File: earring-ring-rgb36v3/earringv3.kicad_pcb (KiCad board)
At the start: 2 copper layers, 108 x 123.5 mm, 70 parts, among them J1 Conn_01x05, Q1 AO3401A, SW1 SW_Push, SW2 SW_Push, U1 GMA2718H09-F42-4P, U2 STM32L031G6Ux

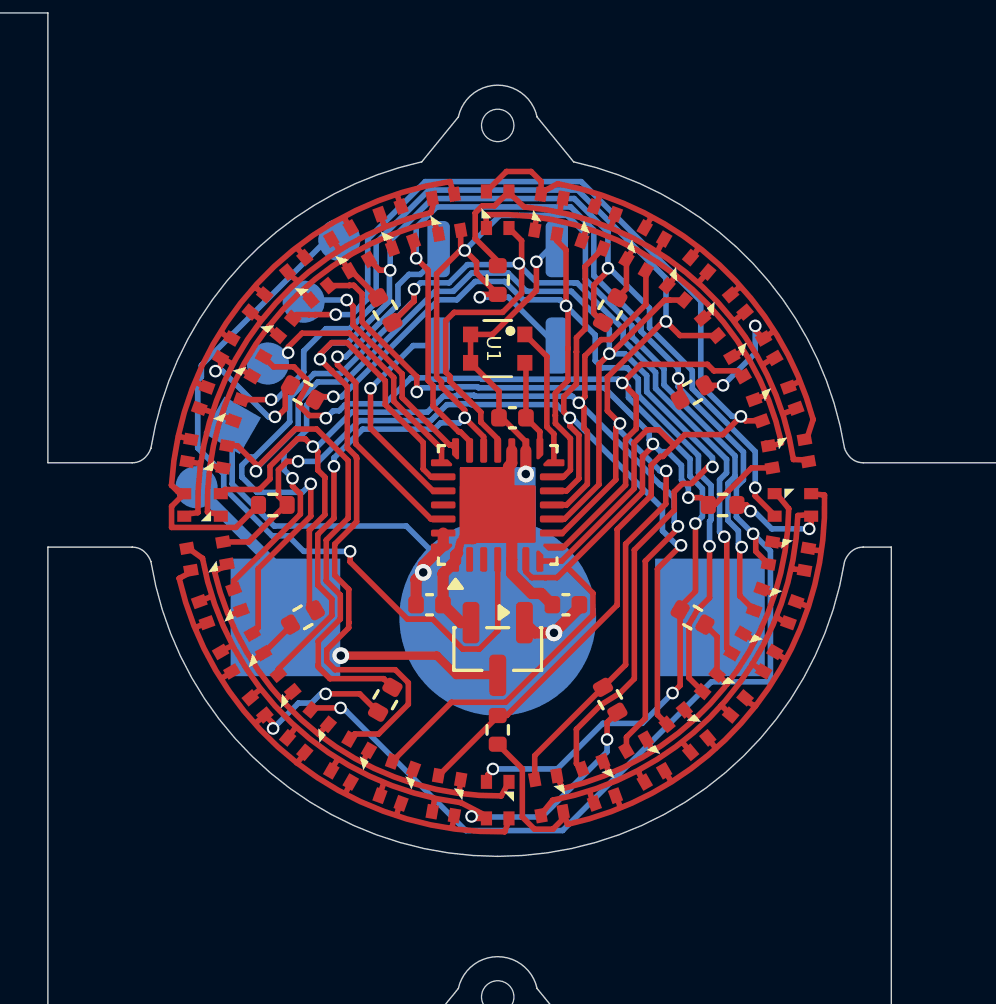
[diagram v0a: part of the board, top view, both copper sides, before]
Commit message: earring-ring-rgb36v3: schematic design for charlieplexing
This is the 3rd or 4th attempt, but the current schematic finally looks
usable.
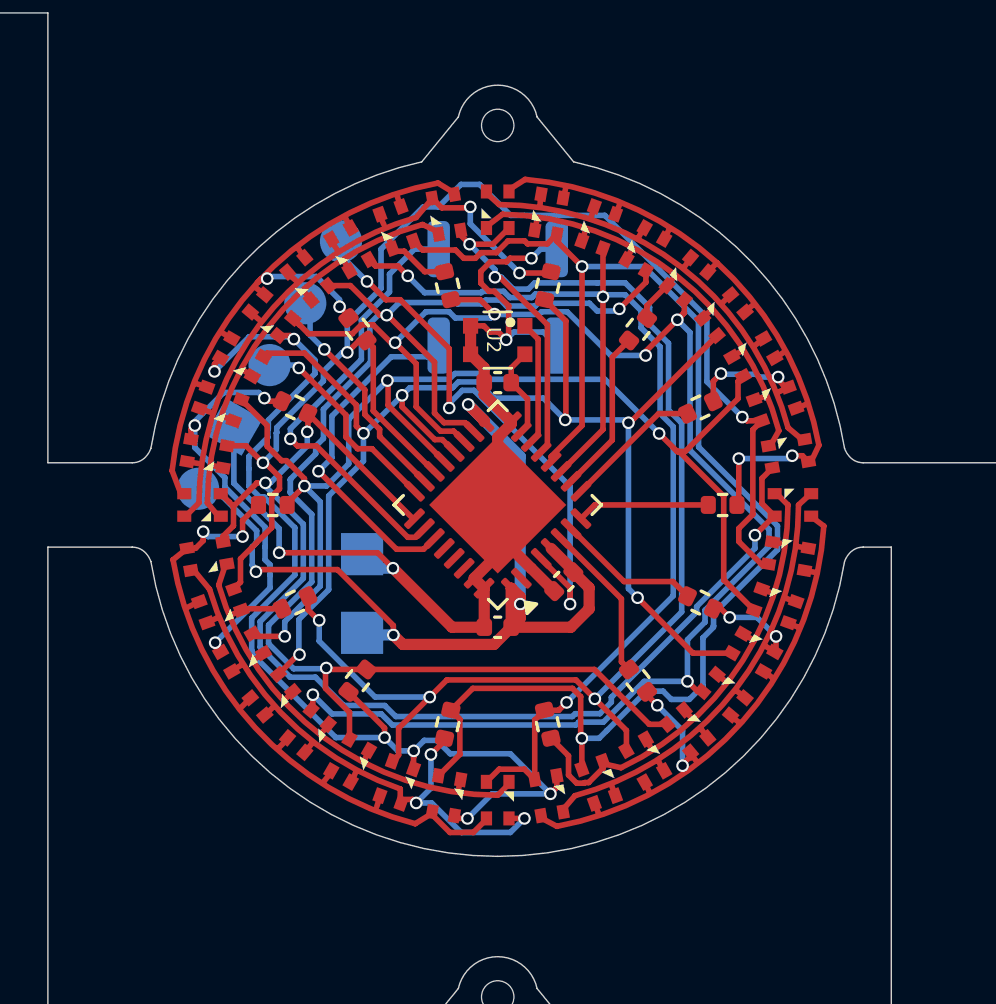
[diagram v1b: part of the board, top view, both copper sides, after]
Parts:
- removed BT1: Battery_Cell, Custom:MY-1220-03
- removed Q1: AO3401A, Package_TO_SOT_SMD:SOT-23
- removed the U2 at (0.00, 0.00)
- added R13: 1.5k, Resistor_SMD:R_0402_1005Metric, F.Cu at (7.21, 3.47)
- added R14: 330, Resistor_SMD:R_0402_1005Metric, F.Cu at (4.99, 6.25)
- added TP1: 3.0V, TestPoint:TestPoint_Pad_1.5x1.5mm, B.Cu at (-4.83, 4.55)
- added TP2: GND, TestPoint:TestPoint_Pad_1.5x1.5mm, B.Cu at (-4.83, 1.75)
- added U1: STM32U073KCUx, Package_DFN_QFN:QFN-32-1EP_5x5mm_P0.5mm_EP3.45x3.45mm, F.Cu at (0.00, 0.00)
- R1, R2: value 1k -> 330
- R10, R11, R4, R5, R7, R8: value 1k -> 1.5k
- R12, R3: value 220 -> 330
- R6, R9: value 220 -> 1.5k
- moved R11 13.5 mm to (7.21, -3.47), turned to 25.71 degrees
- moved R2 12.1 mm to (-4.99, -6.25), turned to 128.57 degrees
- moved R1 11.7 mm to (-7.21, -3.47), turned to 154.29 degrees
- moved R3 11.3 mm to (-8.00, 0.00), turned to 180 degrees
- moved R10 10.4 mm to (4.99, -6.25), turned to 51.43 degrees
- moved R6 6.94 mm to (-4.99, 6.25), turned to -128.57 degrees
- moved R5 6.40 mm to (-1.78, -7.80), turned to 102.86 degrees
- moved R4 5.85 mm to (1.78, -7.80), turned to 77.14 degrees
- moved C1 2.55 mm to (0.00, 4.35)
- moved R8 2.38 mm to (-1.78, 7.80), turned to -102.86 degrees
- moved R9 2.38 mm to (1.78, 7.80), turned to -77.14 degrees
- moved C2 1.36 mm to (0.00, -4.35)
- moved C3 0.83 mm to (2.35, 2.73), turned to -135 degrees
- moved R7 0.60 mm to (-7.21, 3.47), turned to -154.29 degrees
- moved U2 0.31 mm to (0.00, -5.87)
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- renumbered U1 to U2
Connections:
- D1 pad 1: A4 -> A7
- D1 pad 2: A1R -> A10R
- D1 pad 3: A2R -> A11G
- D1 pad 4: A3R -> A12B
- D10 pad 2: A10R -> A9R
- D10 pad 3: A11R -> A13G
- D10 pad 4: A12R -> A14B
- D11 pad 2: A10R -> A9R
- D11 pad 3: A11R -> A13G
- D11 pad 4: A12R -> A14B
- D12 pad 2: A10R -> A9R
- D12 pad 3: A11R -> A13G
- D12 pad 4: A12R -> A14B
- D13 pad 2: A10R -> A9R
- D13 pad 3: A11R -> A13G
- D13 pad 4: A12R -> A14B
- D14 pad 2: A10R -> A9R
- D14 pad 3: A11R -> A13G
- D14 pad 4: A12R -> A14B
- D15 pad 2: A10R -> A9R
- D15 pad 3: A11R -> A13G
- D15 pad 4: A12R -> A14B
- D16 pad 2: A10R -> A9R
- D16 pad 3: A11R -> A13G
- D16 pad 4: A12R -> A14B
- D17 pad 2: A10R -> A9R
- D17 pad 3: A11R -> A13G
- D17 pad 4: A12R -> A14B
- D18 pad 2: A10R -> A6RG
- D18 pad 3: A11R -> A13G
- D18 pad 4: A12R -> A14B
- D19 pad 1: A10 -> A9
- D19 pad 3: A8R -> A8G
- D19 pad 4: A9R -> A3B
- D2 pad 1: A5 -> A8
- D2 pad 2: A1R -> A10R
- D2 pad 3: A2R -> A11G
- D2 pad 4: A3R -> A12B
- D20 pad 1: A11 -> A8
- D20 pad 3: A8R -> A6RG
- D20 pad 4: A9R -> A3B
- D21 pad 1: A12 -> A7
- D21 pad 2: A7R -> A6RG
- D21 pad 3: A8R -> A8G
- D21 pad 4: A9R -> A3B
- D22 pad 1: A1 -> A6
- D22 pad 3: A8R -> A8G
- D22 pad 4: A9R -> A3B
- D23 pad 1: A2 -> A5
- D23 pad 3: A8R -> A8G
- D23 pad 4: A9R -> A3B
- D24 pad 1: A3 -> A4
- D24 pad 3: A8R -> A8G
- D24 pad 4: A9R -> A3B
- D25 pad 1: A4 -> A3
- D25 pad 3: A8R -> A8G
- D25 pad 4: A9R -> A1B
- D26 pad 1: A5 -> A2
- D26 pad 3: A8R -> A8G
- D26 pad 4: A9R -> A3B
- D27 pad 1: A6 -> A1
- D27 pad 3: A8R -> A8G
- D27 pad 4: A9R -> A3B
- D28 pad 1: A7 -> A1
- D28 pad 2: A4R -> A5R
- D28 pad 3: A5R -> A4G
- D28 pad 4: A6R -> A2B
- D29 pad 1: A8 -> A2
- D29 pad 2: A4R -> A5R
- D29 pad 3: A5R -> A4G
- D29 pad 4: A6R -> A1B
- D3 pad 1: A6 -> A9
- D3 pad 2: A1R -> A10R
- D3 pad 3: A2R -> A11G
- D3 pad 4: A3R -> A12B
- D30 pad 1: A9 -> A3
- D30 pad 2: A4R -> A5R
- D30 pad 3: A5R -> A4G
- D30 pad 4: A6R -> A2B
- D31 pad 1: A10 -> A4
- D31 pad 2: A4R -> A5R
- D31 pad 3: A5R -> A6RG
- D31 pad 4: A6R -> A2B
- D32 pad 1: A11 -> A5
- D32 pad 2: A4R -> A6RG
- D32 pad 3: A5R -> A4G
- D32 pad 4: A6R -> A2B
- D33 pad 1: A12 -> A6
- D33 pad 2: A4R -> A5R
- D33 pad 3: A5R -> A4G
- D33 pad 4: A6R -> A2B
- D34 pad 1: A1 -> A9
- D34 pad 2: A4R -> A5R
- D34 pad 3: A5R -> A4G
- D34 pad 4: A6R -> A2B
- D35 pad 1: A2 -> A8
- D35 pad 2: A4R -> A5R
- D35 pad 3: A5R -> A4G
- D35 pad 4: A6R -> A2B
- D36 pad 1: A3 -> A7
- D36 pad 2: A4R -> A5R
- D36 pad 3: A5R -> A4G
- D36 pad 4: A6R -> A2B
- D4 pad 1: A7 -> A6
- D4 pad 2: A1R -> A10R
- D4 pad 3: A2R -> A11G
- D4 pad 4: A3R -> A12B
- D5 pad 1: A8 -> A5
- D5 pad 2: A1R -> A10R
- D5 pad 3: A2R -> A11G
- D5 pad 4: A3R -> A12B
- D6 pad 1: A9 -> A4
- D6 pad 2: A1R -> A10R
- D6 pad 3: A2R -> A11G
- D6 pad 4: A3R -> A12B
- D7 pad 1: A10 -> A3
- D7 pad 2: A1R -> A10R
- D7 pad 3: A2R -> A11G
- D7 pad 4: A3R -> A12B
- D8 pad 1: A11 -> A2
- D8 pad 2: A1R -> A10R
- D8 pad 3: A2R -> A11G
- D8 pad 4: A3R -> A12B
- D9 pad 1: A12 -> A1
- D9 pad 2: A1R -> A10R
- D9 pad 3: A2R -> A11G
- D9 pad 4: A3R -> A12B
- J1 pad 1: VBAT -> VCC
- R1 pad 1: A1R -> A1
- R1 pad 2: A1 -> A1B
- R11 pad 2: A11R -> A11G
- R12 pad 2: A12R -> A12B
- R2 pad 2: A2R -> A2B
- R3 pad 2: A3R -> A3B
- R4 pad 2: A4R -> A4G
- R6 pad 2: A6R -> A6RG
- R8 pad 2: A8R -> A8G
- SW1 pad 2: Net-(U2-PB7) -> BTN_MODE
- SW2 pad 1: A3 -> GND
- SW2 pad 2: Net-(U2-PB3) -> BTN_COLOR
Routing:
- net A11: track 51.4 -> 4.93 mm, vias 2 -> 0
- net A10: track 47.6 -> 5.87 mm, vias 5 -> 0
- net A6RG: track 0.00 -> 38.8 mm, vias 0 -> 6
- net A12: track 40.5 -> 4.73 mm, vias 3 -> 0
- net VCC: track 10.2 -> 33.6 mm, vias 0 -> 4
- net BTN_MODE: track 0.00 -> 15.8 mm, vias 0 -> 1
- net A1B: track 0.00 -> 14.4 mm, vias 0 -> 3
- net VBAT: track 14.1 -> 0.00 mm, vias 1 -> 0
- net Net-(U2-PB7): track 13.9 -> 0.00 mm, vias 1 -> 0
- net A8: track 63.7 -> 50.6 mm, vias 3 -> 2
- net A1: track 56.7 -> 43.9 mm, vias 4 -> 3
- net A6: track 39.0 -> 51.5 mm
- net BTN_COLOR: track 0.00 -> 12.4 mm, vias 0 -> 1
- net A2: track 57.7 -> 48.3 mm, vias 4 -> 3
- net A9: track 50.0 -> 40.7 mm, vias 4 -> 3
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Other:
- board text added: "3V"
- board text added: "G"
- board text added: "TODO: reduce diameter from 25mm to 24.5mm"
- board text added: "v3.0a"
- board text removed: "CR1225"
- board text removed: "v1.2"

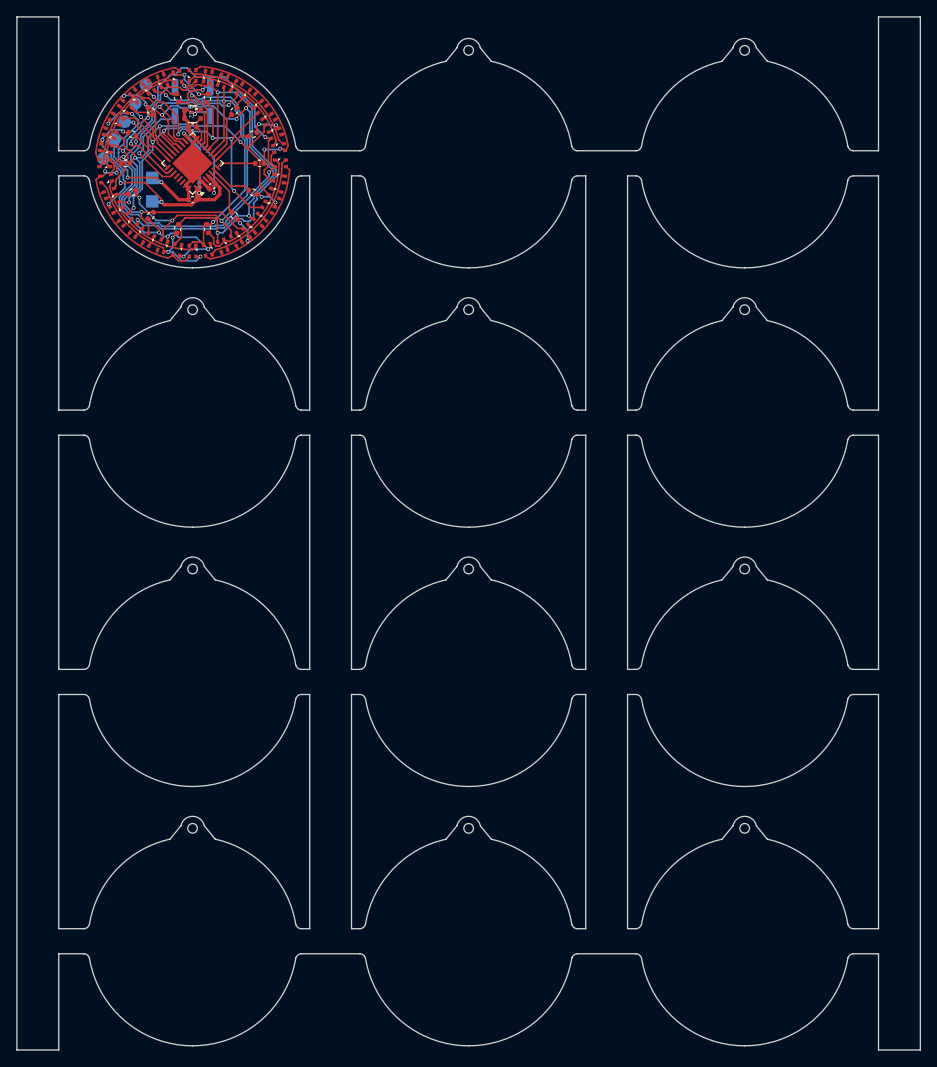
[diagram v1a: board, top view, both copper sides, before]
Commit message: earring-ring-rgb36v3: shrink from 25mm to 24mm
Also use bezier curve for the earring hook ring, this looks much nicer.
And remove the panel, we'll have to recreate it anyway with the smaller
PCB.
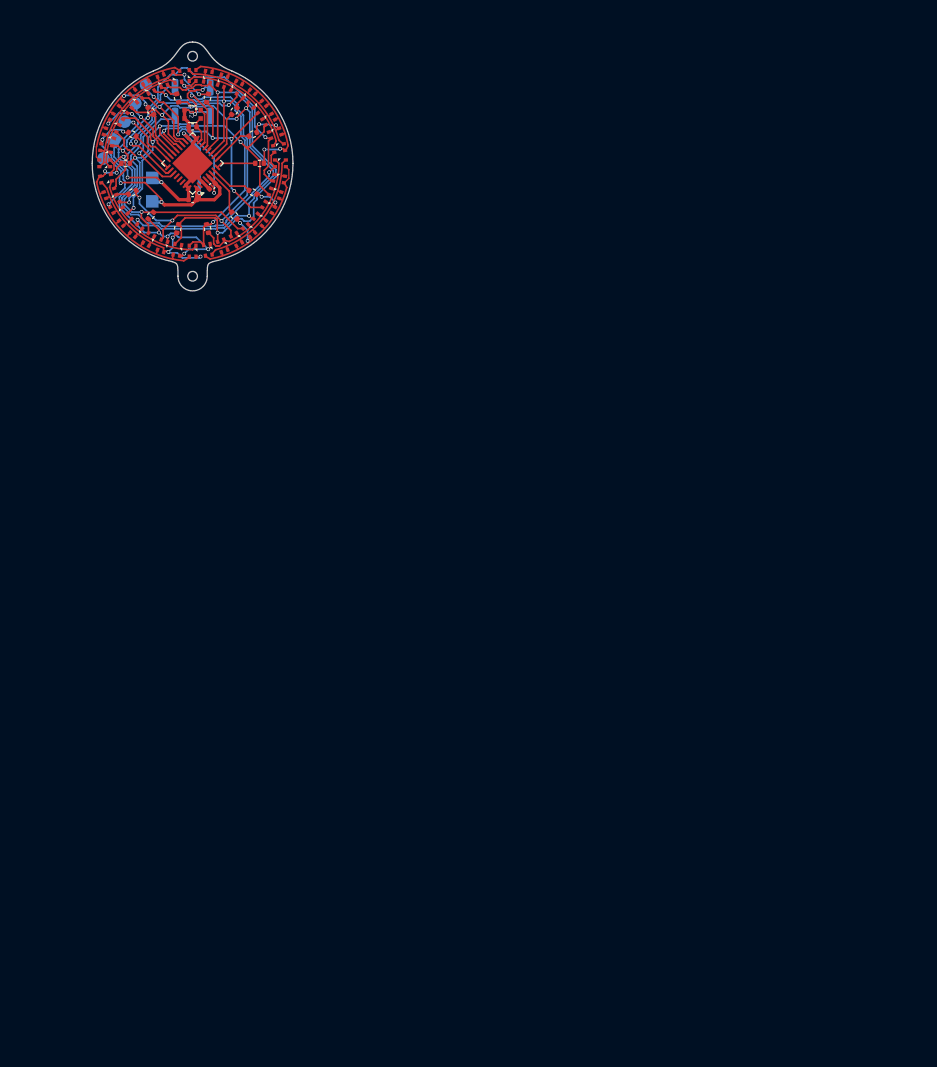
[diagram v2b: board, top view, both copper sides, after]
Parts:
- removed the H1 at (66.0, 17.5)
- removed the H1 at (33.0, 17.5)
- removed the H1 at (33.0, 79.5)
- removed the H1 at (0.00, 48.5)
- removed the H1 at (66.0, 79.5)
- removed the H1 at (33.0, -13.5)
- removed the H1 at (0.00, 79.5)
- removed the H1 at (0.00, 17.5)
- removed the H1 at (66.0, -13.5)
- removed the H1 at (33.0, 48.5)
- removed the H1 at (66.0, 48.5)
- added H1: ToolingHole, Custom:ToolingHole_JLCPCB, F.Cu at (0.00, 13.5)
- moved H1 0.70 mm to (0.00, -12.8)
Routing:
- net A3B: track 6.38 -> 3.85 mm
- net A14B: track 3.66 -> 6.02 mm
- net A2B: track 4.14 -> 5.90 mm
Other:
- board size 108 x 123.5 mm -> 24 x 29.8 mm
- board text added: "color/program"
- board text added: "power"
- board text removed: "TODO: reduce diameter from 25mm to 24.5mm"
- board text removed: "V-cut"
- board text removed: "color/ program"
- board text removed: "mode/power"

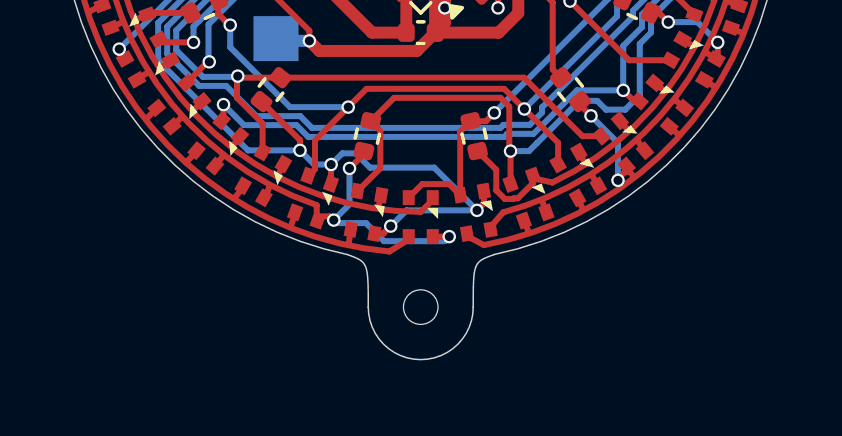
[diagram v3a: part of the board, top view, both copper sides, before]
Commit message: earring-ring-rgb36v3: mouse bytes at bottom tooling hole
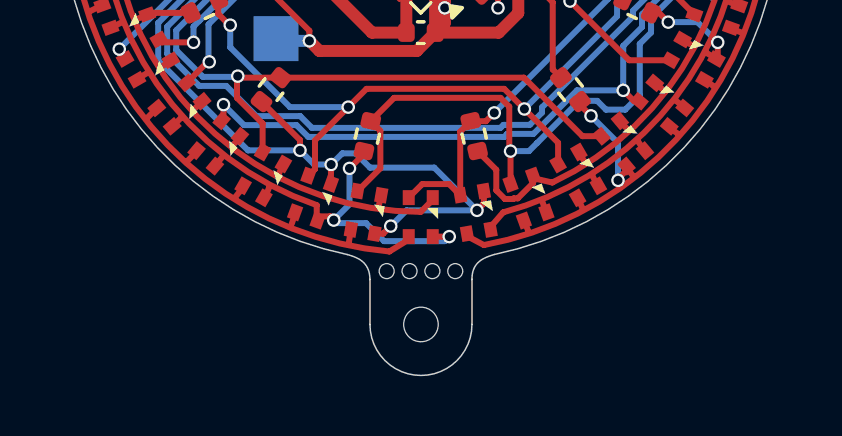
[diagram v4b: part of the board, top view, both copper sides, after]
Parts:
- removed the H1 at (0.00, 13.5)
- added REF**: ToolingHoleWithMouseBytes, Custom:ToolingHoleWithMouseBytes, F.Cu at (0.01, 14.1)
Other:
- board size 24 x 29.8 mm -> 24 x 27.1 mm
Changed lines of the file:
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@@
 		)
 	)
+	(footprint "Custom:ToolingHoleWithMouseBytes"
+		(layer "F.Cu")
+		(at 0.007 14.078)
+		(property "Reference" "REF**"
+			(at 0 -5.1 0)
+			(unlocked yes)
+			(layer "F.SilkS")
+			(hide yes)
+			(effects
+				(font
+					(size 1 1)
+					(thickness 0.1)
+				)
+			)
+		)
+		(property "Value" "ToolingHoleWithMouseBytes"
+			(at 0 -3.6 0)
+			(unlocked yes)
+			(layer "F.Fab")
+			(hide yes)
+			(effects
+				(font
+					(size 1 1)
+					(thickness 0.15)
+				)
+			)
+		)
+		(property "Datasheet" ""
+			(at 0 0 0)
+			(unlocked yes)
+			(layer "F.Fab")
+			(hide yes)
+			(effects
+				(font
+					(size 1 1)
+					(thickness 0.15)
+				)
+			)
+		)
+		(property "Description" ""
+			(at 0 0 0)
+			(unlocked yes)
+			(layer "F.Fab")
+			(hide yes)
+			(effects
+				(font
+					(size 1 1)
+					(thickness 0.15)
+				)
+			)
+		)
+		(attr through_hole board_only)
+		(fp_line
+			(start -1.7 0)
+			(end -1.7 -1.5)
+			(stroke
+				(width 0.05)
+				(type default)
+			)
+			(layer "Edge.Cuts")
+		)
+		(fp_line
+			(start 1.7 0)
+			(end 1.7 -1.5)
+			(stroke
+				(width 0.05)
+				(type default)
+			)
+			(layer "Edge.Cuts")
+		)
+		(fp_arc
+			(start 1.7 0)
+			(mid 0 1.7)
+			(end -1.7 0)
+			(stroke
+				(width 0.05)
+				(type default)
+			)
+			(layer "Edge.Cuts")
+		)
+		(pad "" np_thru_hole circle
+			(at -1.143 -1.778)
+			(size 0.5 0.5)
+			(drill 0.5)
+			(layers "*.Mask")
+		)
+		(pad "" np_thru_hole circle
+			(at -0.381 -1.778)
+			(size 0.5 0.5)
+			(drill 0.5)
+			(layers "*.Mask")
+		)
+		(pad "" np_thru_hole circle
+			(at 0 0)
+			(size 1.152 1.152)
+			(drill 1.152)
+			(layers "*.Mask")
+			(solder_mask_margin 0.148)
+			(clearance 0.248)
+		)
+		(pad "" np_thru_hole circle
+			(at 0.381 -1.778)
+			(size 0.5 0.5)
+			(drill 0.5)
+			(layers "*.Mask")
+		)
+		(pad "" np_thru_hole circle
+			(at 1.143 -1.778)
+			(size 0.5 0.5)
+			(drill 0.5)
+			(layers "*.Mask")
+		)
+		(embedded_fonts no)
+	)
 	(footprint "Custom:NH-Z1415RGBA-SG"
 		(layer "F.Cu")
@@
 		)
 	)
-	(footprint "Custom:ToolingHole_JLCPCB"
-		(layer "F.Cu")
-		(at 0 13.5)
-		(property "Reference" "H1"
-			(at 0 -0.5 0)
-			(unlocked yes)
-			(layer "F.SilkS")
-			(hide yes)
-			(effects
-				(font
-					(size 1 1)
-					(thickness 0.1)
-				)
-			)
-		)
-		(property "Value" "ToolingHole"
-			(at 0 1 0)
-			(unlocked yes)
-			(layer "F.Fab")
-			(hide yes)
-			(effects
-				(font
-					(size 1 1)
-					(thickness 0.15)
-				)
-			)
-		)
-		(property "Datasheet" ""
-			(at 0 0 0)
-			(unlocked yes)
-			(layer "F.Fab")
-			(hide yes)
-			(effects
-				(font
-					(size 1 1)
-					(thickness 0.15)
-				)
-			)
-		)
-		(property "Description" "Mounting Hole without connection"
-			(at 0 0 0)
-			(unlocked yes)
-			(layer "F.Fab")
-			(hide yes)
-			(effects
-				(font
-					(size 1 1)
-					(thickness 0.15)
-				)
-			)
-		)
-		(attr through_hole board_only exclude_from_pos_files exclude_from_bom)
-		(pad "" np_thru_hole circle
-			(at 0 0)
-			(size 1.152 1.152)
-			(drill 1.152)
-			(layers "*.Mask")
-			(solder_mask_margin 0.148)
-			(clearance 0.248)
-		)
-		(embedded_fonts no)
-	)
 	(footprint "Custom:NH-Z1415RGBA-SG"
 		(layer "F.Cu")
@@
 		(end -11.6 3.9)
 		(stroke
-			(width 0.1)
+			(width 0.001)
 			(type default)
 		)
@@
 		(end 11.6 2.7)
 		(stroke
-			(width 0.1)
+			(width 0.001)
 			(type default)
 		)
@@
 	(gr_curve
 		(pts
-			(xy -1.75 13.5) (xy -1.75 12) (xy -1.75 12) (xy -2.447451 11.747764)
+			(xy -1.693 12.578) (xy -1.7 12) (xy -2.086 11.85) (xy -2.447446 11.747765)
 		)
 		(stroke
@@
 		(layer "Edge.Cuts")
 	)
-	(gr_arc
-		(start 1.75 13.5)
-		(mid 0 15.25)
-		(end -1.75 13.5)
-		(stroke
-			(width 0.05)
-			(type default)
-		)
-		(layer "Edge.Cuts")
-	)
 	(gr_curve
 		(pts
-			(xy 1.75 13.5) (xy 1.75 12) (xy 1.75 12) (xy 2.447451 11.747764)
+			(xy 1.707 12.578) (xy 1.7 12) (xy 2.1 11.85) (xy 2.44745 11.747765)
 		)
 		(stroke
